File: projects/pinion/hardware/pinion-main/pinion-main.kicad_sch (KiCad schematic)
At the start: 0 parts

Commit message: [pinion] created sub-sheets
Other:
- added sheet fmu (fmu.kicad_sch)
- added sheet linux (linux.kicad_sch)
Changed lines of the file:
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@@
 	(generator_version "10.0")
 	(paper "A4")
+	(sheet
+		(at 96.52 60.96)
+		(size 39.37 53.34)
+		(exclude_from_sim no)
+		(in_bom yes)
+		(on_board yes)
+		(dnp no)
+		(fields_autoplaced yes)
+		(stroke
+			(width 0.1524)
+			(type solid)
+		)
+		(fill
+			(color 0 0 0 0)
+		)
+		(property "Sheetname" "linux"
+			(at 96.52 60.2484 0)
+			(show_name no)
+			(do_not_autoplace no)
+			(effects
+				(font
+					(size 1.27 1.27)
+				)
+				(justify left bottom)
+			)
+		)
+		(property "Sheetfile" "linux.kicad_sch"
+			(at 96.52 114.8846 0)
+			(show_name no)
+			(do_not_autoplace no)
+			(effects
+				(font
+					(size 1.27 1.27)
+				)
+				(justify left top)
+			)
+		)
+		(instances
+			(project "pinion-main"
+				(path "/6c7907f5-5439-4f54-a5a2-0a7e85489635"
+					(page "3")
+				)
+			)
+		)
+	)
+	(sheet
+		(at 198.12 68.58)
+		(size 49.53 35.56)
+		(exclude_from_sim no)
+		(in_bom yes)
+		(on_board yes)
+		(dnp no)
+		(fields_autoplaced yes)
+		(stroke
+			(width 0.1524)
+			(type solid)
+		)
+		(fill
+			(color 0 0 0 0)
+		)
+		(property "Sheetname" "fmu"
+			(at 198.12 67.8684 0)
+			(show_name no)
+			(do_not_autoplace no)
+			(effects
+				(font
+					(size 1.27 1.27)
+				)
+				(justify left bottom)
+			)
+		)
+		(property "Sheetfile" "fmu.kicad_sch"
+			(at 198.12 104.7246 0)
+			(show_name no)
+			(do_not_autoplace no)
+			(effects
+				(font
+					(size 1.27 1.27)
+				)
+				(justify left top)
+			)
+		)
+		(instances
+			(project "pinion-main"
+				(path "/6c7907f5-5439-4f54-a5a2-0a7e85489635"
+					(page "2")
+				)
+			)
+		)
+	)
 	(sheet_instances
 		(path "/"

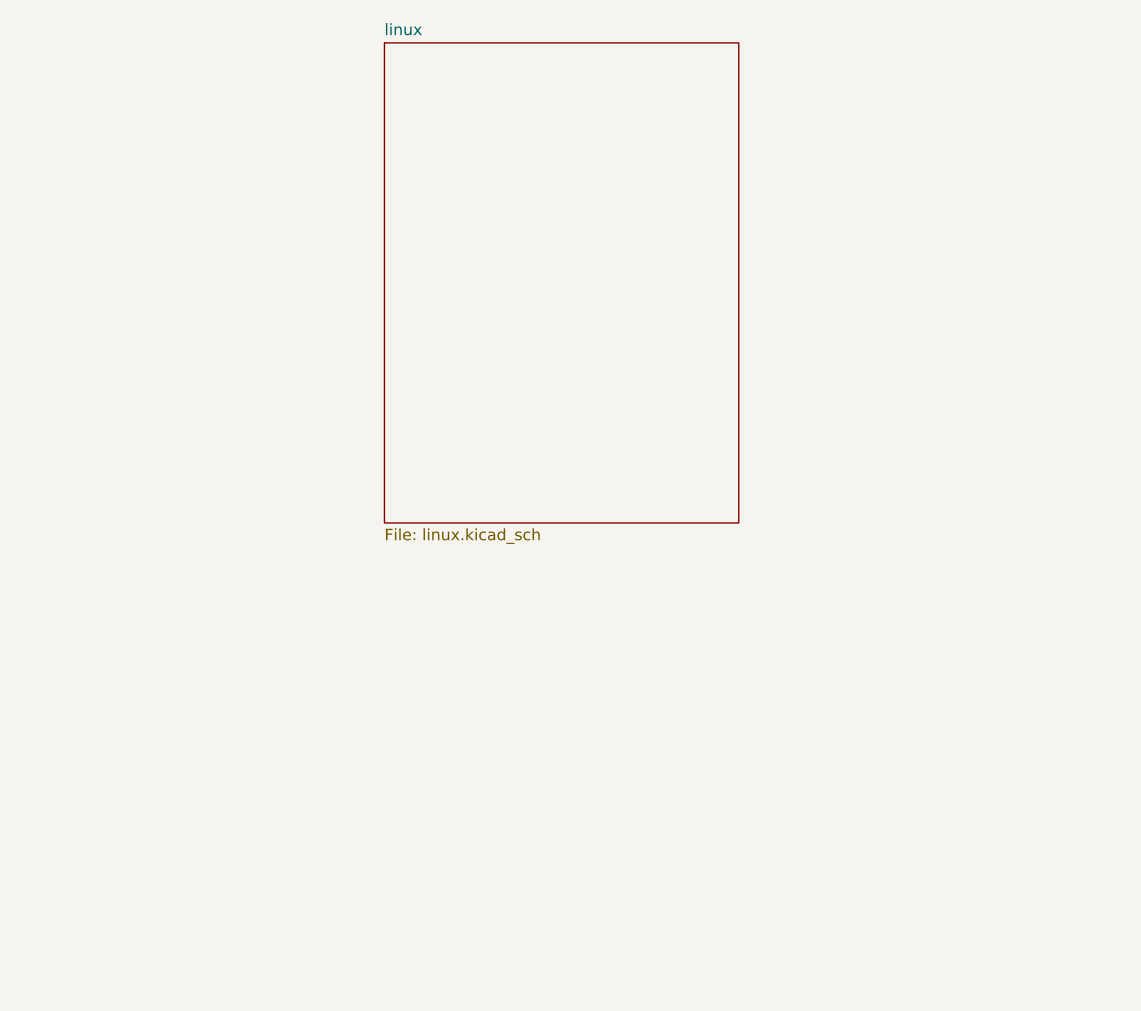
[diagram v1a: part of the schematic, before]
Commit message: [pinion] added 5v input power
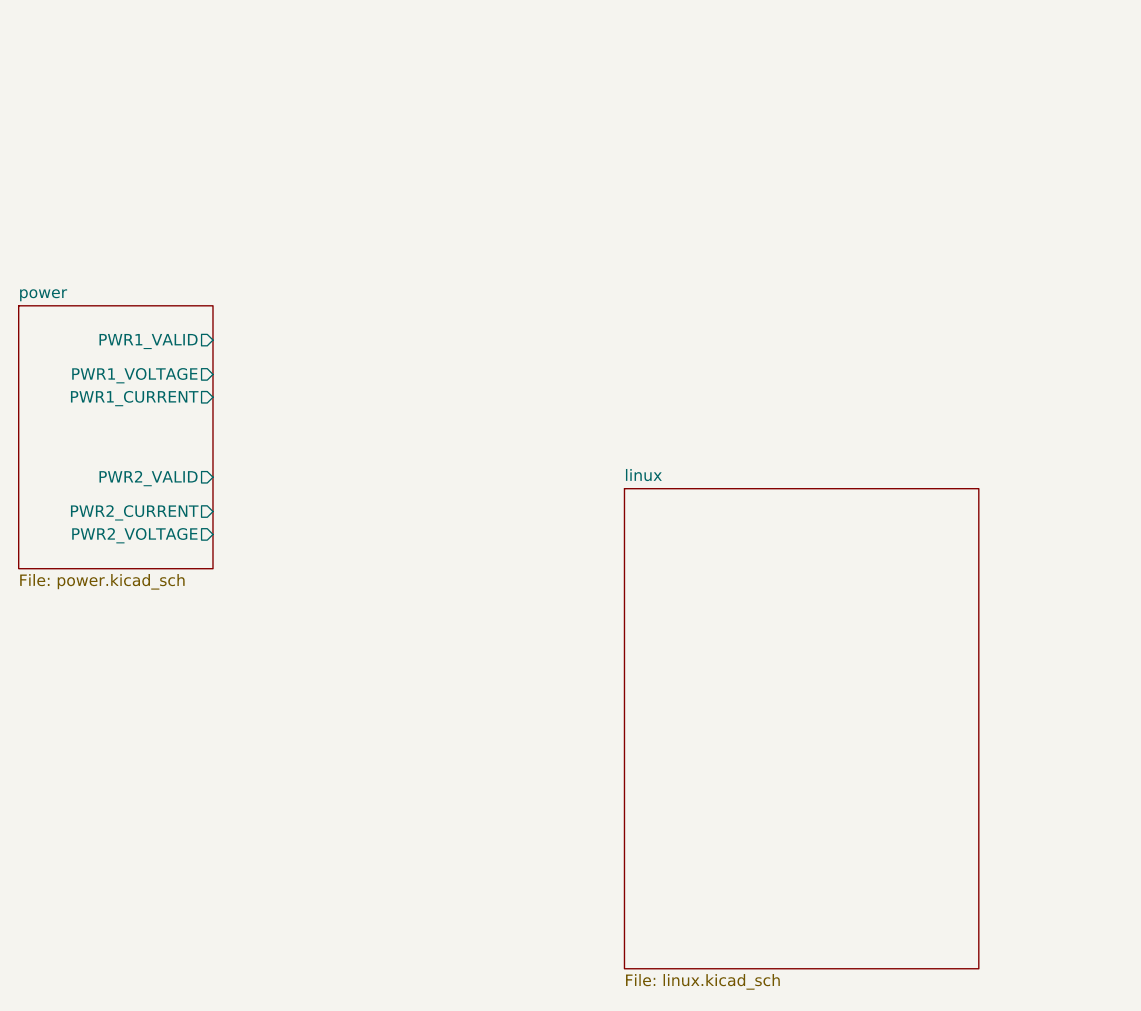
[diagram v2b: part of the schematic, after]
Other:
- added sheet power (power.kicad_sch)
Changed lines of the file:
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@@
 	(paper "A4")
 	(sheet
-		(at 96.52 60.96)
+		(at 123.19 110.49)
 		(size 39.37 53.34)
 		(exclude_from_sim no)
@@
 		)
 		(property "Sheetname" "linux"
-			(at 96.52 60.2484 0)
+			(at 123.19 109.7784 0)
 			(show_name no)
 			(do_not_autoplace no)
@@
 		)
 		(property "Sheetfile" "linux.kicad_sch"
-			(at 96.52 114.8846 0)
+			(at 123.19 164.4146 0)
 			(show_name no)
 			(do_not_autoplace no)
@@
 				)
 			)
+		)
+	)
+	(sheet
+		(at 55.88 90.17)
+		(size 21.59 29.21)
+		(exclude_from_sim no)
+		(in_bom yes)
+		(on_board yes)
+		(dnp no)
+		(fields_autoplaced yes)
+		(stroke
+			(width 0.1524)
+			(type solid)
+		)
+		(fill
+			(color 0 0 0 0)
+		)
+		(property "Sheetname" "power"
+			(at 55.88 89.4584 0)
+			(show_name no)
+			(do_not_autoplace no)
+			(effects
+				(font
+					(size 1.27 1.27)
+				)
+				(justify left bottom)
+			)
+		)
+		(property "Sheetfile" "power.kicad_sch"
+			(at 55.88 119.9646 0)
+			(show_name no)
+			(do_not_autoplace no)
+			(effects
+				(font
+					(size 1.27 1.27)
+				)
+				(justify left top)
+			)
+		)
+		(pin "PWR1_VALID" output
+			(at 77.47 93.98 0)
+			(effects
+				(font
+					(size 1.27 1.27)
+				)
+				(justify right)
+			)
+		)
+		(pin "PWR1_VOLTAGE" output
+			(at 77.47 97.79 0)
+			(effects
+				(font
+					(size 1.27 1.27)
+				)
+				(justify right)
+			)
+		)
+		(pin "PWR1_CURRENT" output
+			(at 77.47 100.33 0)
+			(effects
+				(font
+					(size 1.27 1.27)
+				)
+				(justify right)
+			)
+		)
+		(pin "PWR2_CURRENT" output
+			(at 77.47 113.03 0)
+			(effects
+				(font
+					(size 1.27 1.27)
+				)
+				(justify right)
+			)
+		)
+		(pin "PWR2_VALID" output
+			(at 77.47 109.22 0)
+			(effects
+				(font
+					(size 1.27 1.27)
+				)
+				(justify right)
+			)
+		)
+		(pin "PWR2_VOLTAGE" output
+			(at 77.47 115.57 0)
+			(effects
+				(font
+					(size 1.27 1.27)
+				)
+				(justify right)
+			)
+		)
+		(instances
+			(project "pinion-main"
+				(path "/6c7907f5-5439-4f54-a5a2-0a7e85489635"
+					(page "19")
+				)
+			)

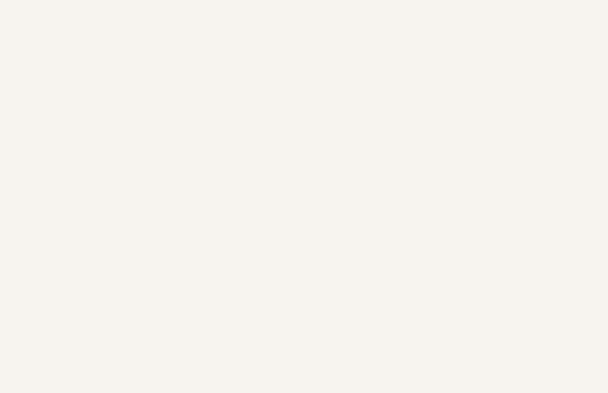
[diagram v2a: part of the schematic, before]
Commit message: [pinion] added 30.5x30.5 mounting holes
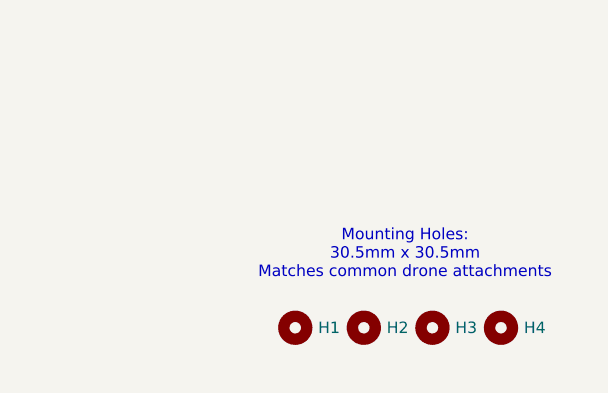
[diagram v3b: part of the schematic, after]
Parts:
- added H1, H2, H3, H4: MountingHole, MountingHole:MountingHole_3.2mm_M3, symbol Mechanical:MountingHole
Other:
- note added: "Mounting Holes: 30.5mm x 30.5mm Matches common drone attachments"

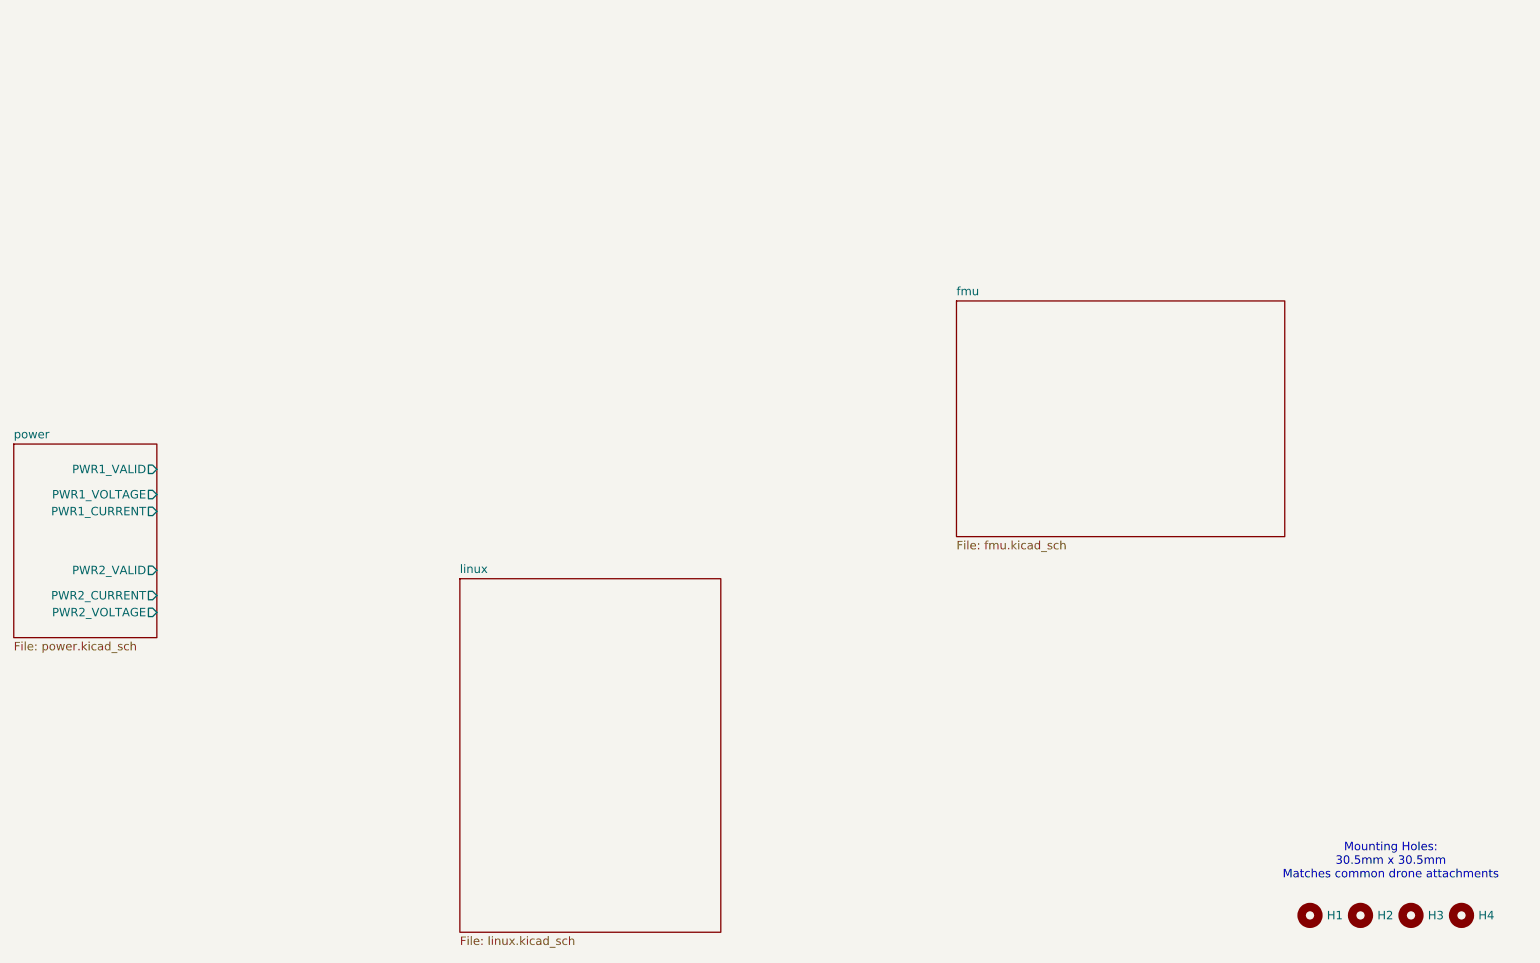
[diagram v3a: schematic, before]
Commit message: [pinion] 3v3 power for sys and fmu
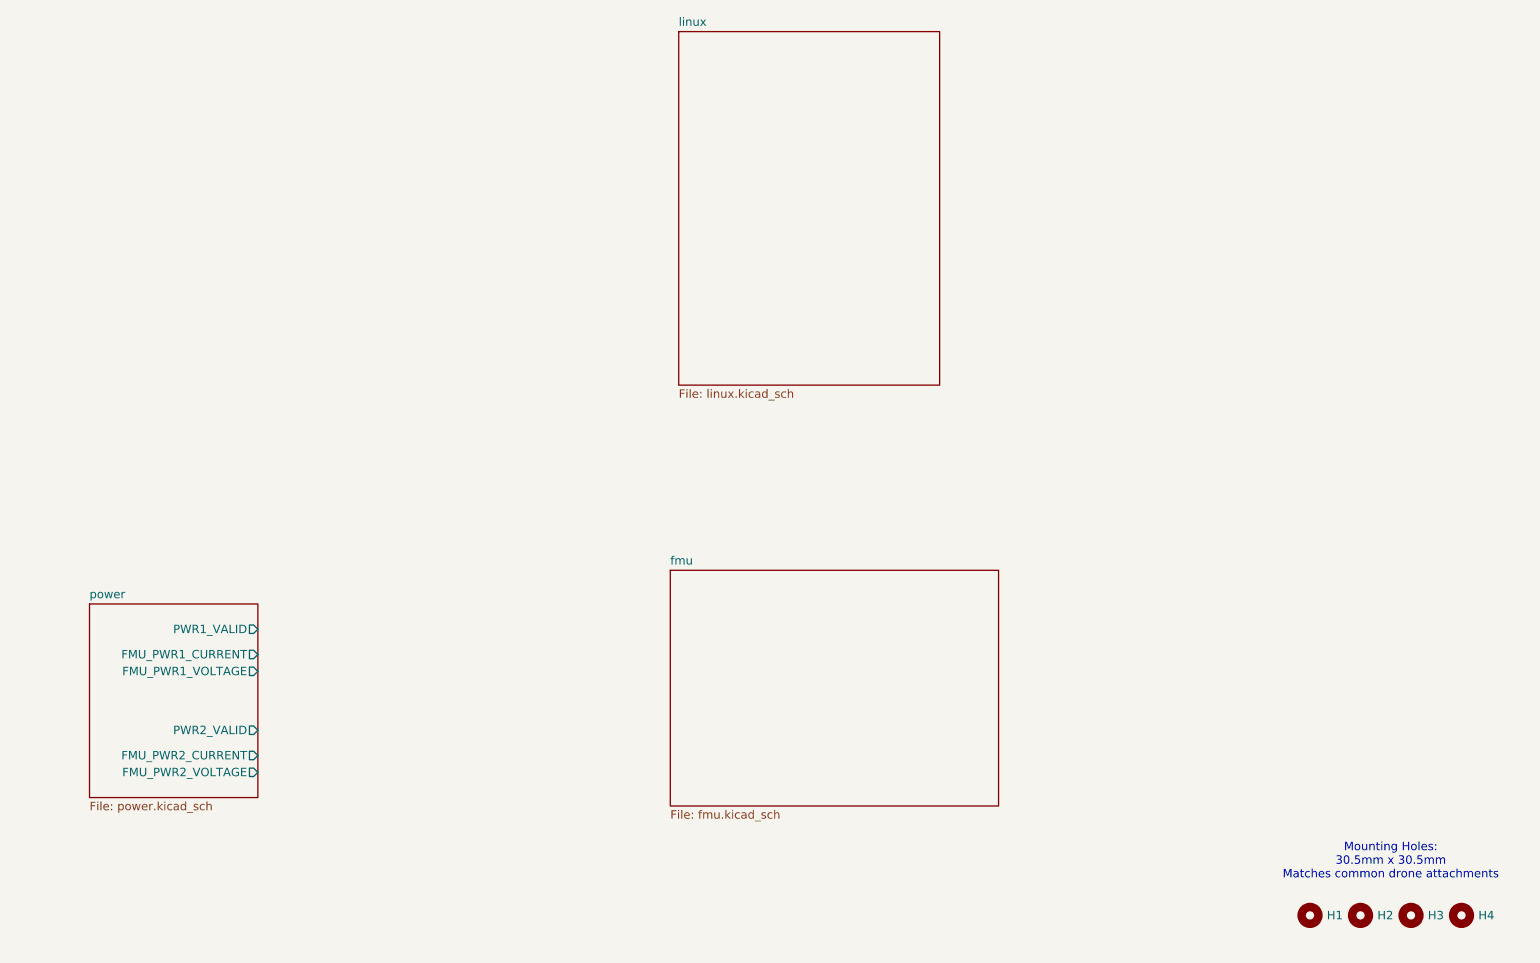
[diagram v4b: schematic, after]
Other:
- sheet power ports: added FMU_PWR1_CURRENT, FMU_PWR1_VOLTAGE, FMU_PWR2_CURRENT, FMU_PWR2_VOLTAGE; removed PWR1_CURRENT, PWR1_VOLTAGE, PWR2_CURRENT, PWR2_VOLTAGE
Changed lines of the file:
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@@
 	)
 	(sheet
-		(at 123.19 110.49)
+		(at 156.21 27.94)
 		(size 39.37 53.34)
 		(exclude_from_sim no)
@@
 		)
 		(property "Sheetname" "linux"
-			(at 123.19 109.7784 0)
+			(at 156.21 27.2284 0)
 			(show_name no)
 			(do_not_autoplace no)
@@
 		)
 		(property "Sheetfile" "linux.kicad_sch"
-			(at 123.19 164.4146 0)
+			(at 156.21 81.8646 0)
 			(show_name no)
 			(do_not_autoplace no)
@@
 	)
 	(sheet
-		(at 198.12 68.58)
+		(at 154.94 109.22)
 		(size 49.53 35.56)
 		(exclude_from_sim no)
@@
 		)
 		(property "Sheetname" "fmu"
-			(at 198.12 67.8684 0)
+			(at 154.94 108.5084 0)
 			(show_name no)
 			(do_not_autoplace no)
@@
 		)
 		(property "Sheetfile" "fmu.kicad_sch"
-			(at 198.12 104.7246 0)
+			(at 154.94 145.3646 0)
 			(show_name no)
 			(do_not_autoplace no)
@@
 	)
 	(sheet
-		(at 55.88 90.17)
-		(size 21.59 29.21)
+		(at 67.31 114.3)
+		(size 25.4 29.21)
 		(exclude_from_sim no)
 		(in_bom yes)
@@
 		)
 		(property "Sheetname" "power"
-			(at 55.88 89.4584 0)
+			(at 67.31 113.5884 0)
 			(show_name no)
 			(do_not_autoplace no)
@@
 		)
 		(property "Sheetfile" "power.kicad_sch"
-			(at 55.88 119.9646 0)
+			(at 67.31 144.0946 0)
 			(show_name no)
 			(do_not_autoplace no)
@@
 		)
 		(pin "PWR1_VALID" output
-			(at 77.47 93.98 0)
-			(effects
-				(font
-					(size 1.27 1.27)
-				)
-				(justify right)
-			)
-		)
-		(pin "PWR1_VOLTAGE" output
-			(at 77.47 97.79 0)
-			(effects
-				(font
-					(size 1.27 1.27)
-				)
-				(justify right)
-			)
-		)
-		(pin "PWR1_CURRENT" output
-			(at 77.47 100.33 0)
-			(effects
-				(font
-					(size 1.27 1.27)
-				)
-				(justify right)
-			)
-		)
-		(pin "PWR2_CURRENT" output
-			(at 77.47 113.03 0)
+			(at 92.71 118.11 0)
 			(effects
 				(font
@@
 		)
 		(pin "PWR2_VALID" output
-			(at 77.47 109.22 0)
+			(at 92.71 133.35 0)
 			(effects
 				(font
@@
 			)
 		)
-		(pin "PWR2_VOLTAGE" output
-			(at 77.47 115.57 0)
+		(pin "FMU_PWR2_CURRENT" output
+			(at 92.71 137.16 0)
 			(effects
 				(font
+					(size 1.27 1.27)
+				)
+				(justify right)
+			)
+		)
+		(pin "FMU_PWR2_VOLTAGE" output
+			(at 92.71 139.7 0)
+			(effects
+				(font
+					(size 1.27 1.27)
+				)
+				(justify right)
+			)
+		)
+		(pin "FMU_PWR1_VOLTAGE" output
+			(at 92.71 124.46 0)
+			(effects
+				(font
+					(size 1.27 1.27)
+				)
+				(justify right)
+			)
+		)
+		(pin "FMU_PWR1_CURRENT" output
+			(at 92.71 121.92 0)
+			(effects
+				(font
